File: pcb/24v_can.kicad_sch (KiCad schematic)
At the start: 8 parts, among them J19 Conn_01x02_Pin, J20 MX3.0, J21 MX3.0, U16 SN65HVD231, U23 SMF05CT1G-ES

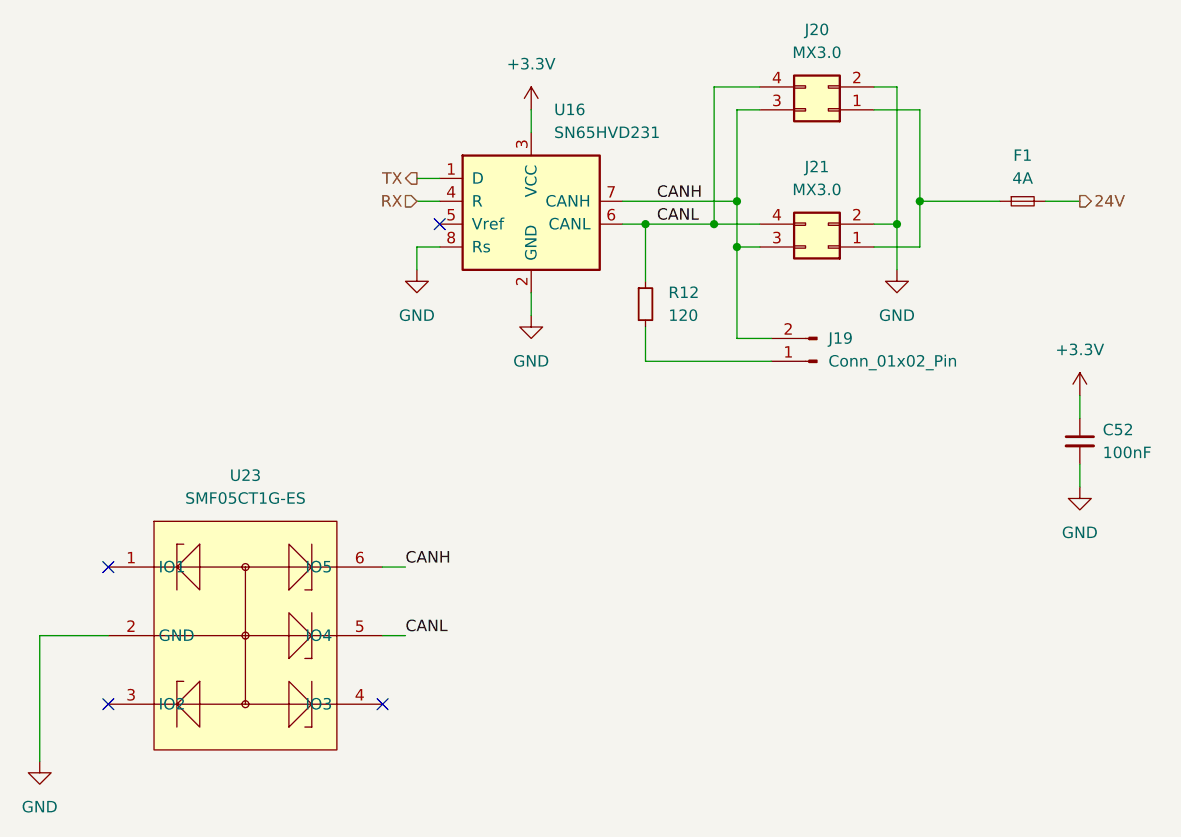
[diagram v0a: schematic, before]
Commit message: fixes #18 fixes #26
replace usb-c connector
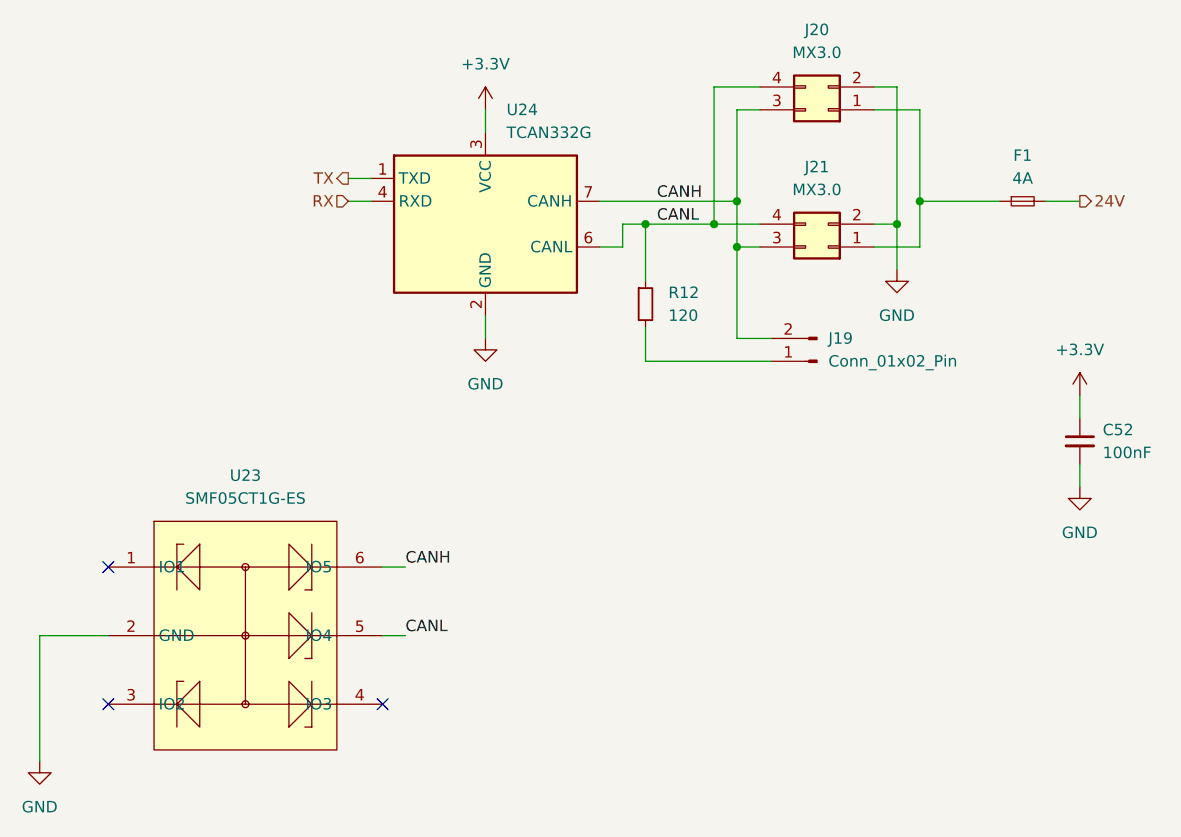
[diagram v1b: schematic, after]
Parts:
- removed U16: SN65HVD231, Package_SO:SOIC-8_3.9x4.9mm_P1.27mm, symbol Interface_CAN_LIN:SN65HVD231
- added U24: TCAN332G, Package_SO:SOIC-8_3.9x4.9mm_P1.27mm, symbol Interface_CAN_LIN:TCAN332G
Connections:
- net +3.3V: now also U24.3 (VCC)
- net CANH: now also U24.7 (CANH)
- net CANL: now also U24.6 (CANL)
- net GND: now also U24.2 (GND)
- net RX: now also U24.4 (RXD)
- net TX: now also U24.1 (TXD)
- no-connect marks 4 -> 3
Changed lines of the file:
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@@
-	)
-	(no_connect
-		(at 67.31 54.61)
 	)
 	(no_connect
@@
 	(wire
 		(pts
-			(xy 77.47 41.91) (xy 77.47 44.45)
+			(xy 85.09 52.07) (xy 100.33 52.07)
+		)
+		(stroke
+			(width 0)
+			(type default)
+		)
+	)
+	(wire
+		(pts
+			(xy 72.39 41.91) (xy 72.39 44.45)
 		)
 		(stroke
@@
 	(wire
 		(pts
-			(xy 64.77 52.07) (xy 67.31 52.07)
+			(xy 57.15 52.07) (xy 59.69 52.07)
+		)
+		(stroke
+			(width 0)
+			(type default)
+		)
+	)
+	(wire
+		(pts
+			(xy 87.63 57.15) (xy 87.63 54.61)
 		)
 		(stroke
@@
 	(wire
 		(pts
-			(xy 64.77 59.69) (xy 64.77 57.15)
-		)
-		(stroke
-			(width 0)
-			(type default)
-		)
-	)
-	(wire
-		(pts
 			(xy 118.11 39.37) (xy 115.57 39.37)
 		)
@@
 	(wire
 		(pts
-			(xy 64.77 49.53) (xy 67.31 49.53)
+			(xy 57.15 49.53) (xy 59.69 49.53)
 		)
 		(stroke
@@
 	(wire
 		(pts
-			(xy 87.63 52.07) (xy 100.33 52.07)
-		)
-		(stroke
-			(width 0)
-			(type default)
-		)
-	)
-	(wire
-		(pts
 			(xy 115.57 54.61) (xy 118.11 54.61)
 		)
@@
 	(wire
 		(pts
+			(xy 85.09 57.15) (xy 87.63 57.15)
+		)
+		(stroke
+			(width 0)
+			(type default)
+		)
+	)
+	(wire
+		(pts
 			(xy 120.65 52.07) (xy 129.54 52.07)
 		)
@@
 	(wire
 		(pts
-			(xy 77.47 62.23) (xy 77.47 64.77)
+			(xy 72.39 64.77) (xy 72.39 67.31)
 		)
 		(stroke
@@
 		(pts
 			(xy 90.17 69.85) (xy 104.14 69.85)
-		)
-		(stroke
-			(width 0)
-			(type default)
-		)
-	)
-	(wire
-		(pts
-			(xy 64.77 57.15) (xy 67.31 57.15)
 		)
 		(stroke
@@
 	(hierarchical_label "RX"
 		(shape input)
-		(at 64.77 52.07 180)
+		(at 57.15 52.07 180)
 		(effects
 			(font
@@
 	(hierarchical_label "TX"
 		(shape output)
-		(at 64.77 49.53 180)
+		(at 57.15 49.53 180)
 		(effects
 			(font
@@
 	(symbol
 		(lib_id "power:GND")
-		(at 77.47 64.77 0)
+		(at 72.39 67.31 0)
 		(unit 1)
 		(exclude_from_sim no)
@@
 		(fields_autoplaced yes)
 		(property "Reference" "#PWR0127"
-			(at 77.47 71.12 0)
+			(at 72.39 73.66 0)
 			(effects
 				(font
@@
 		)
 		(property "Value" "GND"
-			(at 77.47 69.85 0)
+			(at 72.39 72.39 0)
 			(effects
 				(font
@@
 		)
 		(property "Footprint" ""
-			(at 77.47 64.77 0)
+			(at 72.39 67.31 0)
 			(effects
 				(font
@@
 		)
 		(property "Datasheet" ""
-			(at 77.47 64.77 0)
+			(at 72.39 67.31 0)
 			(effects
 				(font
@@
 		)
 		(property "Description" "Power symbol creates a global label with name \"GND\" , ground"
-			(at 77.47 64.77 0)
+			(at 72.39 67.31 0)
 			(effects
 				(font
@@
 	)
 	(symbol
-		(lib_id "Interface_CAN_LIN:SN65HVD231")
-		(at 77.47 52.07 0)
+		(lib_id "Interface_CAN_LIN:TCAN332G")
+		(at 72.39 54.61 0)
 		(unit 1)
 		(exclude_from_sim no)
@@
 		(dnp no)
 		(fields_autoplaced yes)
-		(property "Reference" "U16"
-			(at 80.0118 41.91 0)
+		(property "Reference" "U24"
+			(at 74.7296 41.91 0)
 			(effects
 				(font
@@
 			)
 		)
-		(property "Value" "SN65HVD231"
-			(at 80.0118 44.45 0)
+		(property "Value" "TCAN332G"
+			(at 74.7296 44.45 0)
 			(effects
 				(font
@@
 		)
 		(property "Footprint" "Package_SO:SOIC-8_3.9x4.9mm_P1.27mm"
-			(at 77.47 64.77 0)
-			(effects
-				(font
-					(size 1.27 1.27)
-				)
-				(hide yes)
-			)
-		)
-		(property "Datasheet" "http://www.ti.com/lit/ds/symlink/sn65hvd230.pdf"
-			(at 74.93 41.91 0)
-			(effects
-				(font
-					(size 1.27 1.27)
-				)
-				(hide yes)
-			)
-		)
-		(property "Description" "CAN Bus Transceivers, 3.3V, 1Mbps,Ultra Low-Power capabilities, SOIC-8"
-			(at 77.47 52.07 0)
-			(effects
-				(font
-					(size 1.27 1.27)
-				)
-				(hide yes)
-			)
-		)
-		(property "LCSC" "C129257"
-			(at 80.0118 41.91 0)
-			(effects
-				(font
-					(size 1.27 1.27)
-				)
-				(hide yes)
-			)
+			(at 72.39 67.31 0)
+			(effects
+				(font
+					(size 1.27 1.27)
+					(italic yes)
+				)
+				(hide yes)
+			)
+		)
+		(property "Datasheet" "http://www.ti.com/lit/ds/symlink/tcan337.pdf"
+			(at 72.39 54.61 0)
+			(effects
+				(font
+					(size 1.27 1.27)
+				)
+				(hide yes)
+			)
+		)
+		(property "Description" "High-Speed CAN Transceiver with CAN FD, 5Mbps, 3.3V supply, SOT-23-8/SOIC-8"
+			(at 72.39 54.61 0)
+			(effects
+				(font
+					(size 1.27 1.27)
+				)
+				(hide yes)
+			)
+		)
+		(property "LCSC" "C191010"
+			(at 74.7296 41.91 0)
+			(effects
+				(font
+					(size 1.27 1.27)
+				)
+				(hide yes)
+			)
+		)
+		(pin "6"
+		)
+		(pin "7"
+		)
+		(pin "1"
 		)
 		(pin "4"
 		)
-		(pin "7"
+		(pin "5"
+		)
+		(pin "8"
 		)
 		(pin "3"
 		)
-		(pin "8"
-		)
-		(pin "6"
-		)
-		(pin "5"
-		)
 		(pin "2"
-		)
-		(pin "1"
 		)
 		(instances
 			(project ""
 				(path "/0a1f9f3d-7c96-45bd-a844-76a0eed80de7/bcca0dfa-61ce-42fe-a001-8a8039602384"
-					(reference "U16")
+					(reference "U24")
 					(unit 1)
 				)
@@
 	(symbol
 		(lib_id "power:+3.3V")
-		(at 77.47 41.91 0)
+		(at 72.39 41.91 0)
 		(unit 1)
 		(exclude_from_sim no)
@@
 		(fields_autoplaced yes)
 		(property "Reference" "#PWR0126"
-			(at 77.47 45.72 0)
+			(at 72.39 45.72 0)
 			(effects
 				(font
@@
 		)
 		(property "Value" "+3.3V"
-			(at 77.47 36.83 0)
+			(at 72.39 36.83 0)
 			(effects
 				(font
@@
 		)
 		(property "Footprint" ""
-			(at 77.47 41.91 0)
+			(at 72.39 41.91 0)
 			(effects
 				(font
@@
 		)
 		(property "Datasheet" ""
-			(at 77.47 41.91 0)
+			(at 72.39 41.91 0)
 			(effects
 				(font
@@
 		)
 		(property "Description" "Power symbol creates a global label with name \"+3.3V\""
-			(at 77.47 41.91 0)
+			(at 72.39 41.91 0)
 			(effects
 				(font
@@
 					(unit 1)
 				)
-			)
-		)
-	)
-	(symbol
-		(lib_id "power:GND")
-		(at 64.77 59.69 0)
-		(unit 1)
-		(exclude_from_sim no)
-		(in_bom yes)
-		(on_board yes)
-		(dnp no)
-		(fields_autoplaced yes)
-		(property "Reference" "#PWR0125"
-			(at 64.77 66.04 0)
-			(effects
-				(font
-					(size 1.27 1.27)
-				)
-				(hide yes)
-			)
-		)
-		(property "Value" "GND"
-			(at 64.77 64.77 0)
-			(effects
-				(font
-					(size 1.27 1.27)
-				)
-			)
-		)
-		(property "Footprint" ""
-			(at 64.77 59.69 0)
-			(effects
-				(font
-					(size 1.27 1.27)
-				)
-				(hide yes)
-			)
-		)
-		(property "Datasheet" ""
-			(at 64.77 59.69 0)
-			(effects
-				(font
-					(size 1.27 1.27)
-				)
-				(hide yes)
-			)
-		)
-		(property "Description" "Power symbol creates a global label with name \"GND\" , ground"
-			(at 64.77 59.69 0)
-			(effects
-				(font
-					(size 1.27 1.27)
-				)
-				(hide yes)
-			)
-		)
-		(pin "1"
-		)
-		(instances
-			(project "turtleboard"
-				(path "/0a1f9f3d-7c96-45bd-a844-76a0eed80de7/bcca0dfa-61ce-42fe-a001-8a8039602384"
-					(reference "#PWR0125")
-					(unit 1)
-				)
